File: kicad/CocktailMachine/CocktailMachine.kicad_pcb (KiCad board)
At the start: 2 copper layers, 104.1 x 84.4 mm, 70 parts, among them J1 Conn_01x08_Male, J2 0022232041, J3 3220-10-0100-00, J4 Barrel_Jack_Switch, J5 105-1102-001, J6 105-1103-001, J7 0022232041, U1 ESP32-WROOM-32, U2 TXB0104PWR, U3 MCP6477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

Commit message: Add gerber and drill files
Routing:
- net GND1: track 74.6 -> 74.0 mm
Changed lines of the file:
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@@
       (psa4output false)
       (plotreference true)
-      (plotvalue true)
+      (plotvalue false)
       (plotinvisibletext false)
       (sketchpadsonfab false)
@@
       (outputformat 1)
       (mirror false)
-      (drillshape 1)
+      (drillshape 0)
       (scaleselection 1)
-      (outputdirectory "")
+      (outputdirectory "gerber/")
     )
   )
@@
     (pad "" np_thru_hole circle locked (at 2.046701 4.700001) (size 0.9906 0.9906) (drill 0.9906) (layers *.Cu *.Mask))
     (pad "" np_thru_hole circle locked (at 4.053301 4.700001) (size 0.9906 0.9906) (drill 0.9906) (layers *.Cu *.Mask))
-    (pad "1" thru_hole oval locked (at 6.000001 0 90) (size 4.0132 1.4986) (drill oval 2.7 0.4) (layers *.Cu *.Mask)
+    (pad "1" thru_hole oval locked (at 6.000001 0 90) (size 4.0132 1.4986) (drill oval 2.7 0.4572) (layers *.Cu *.Mask)
       (net 7 "+12V") (pintype "passive"))
-    (pad "2" thru_hole oval locked (at 0 0 90) (size 3.5052 1.4986) (drill oval 2.7 0.4) (layers *.Cu *.Mask)
+    (pad "2" thru_hole oval locked (at 0 0 90) (size 3.5052 1.4986) (drill oval 2.7 0.4572) (layers *.Cu *.Mask)
       (net 6 "GND1") (pintype "passive"))
-    (pad "3" thru_hole oval locked (at 3.050001 4.700001) (size 3.5052 1.4986) (drill oval 2.7 0.4) (layers *.Cu *.Mask)
+    (pad "3" thru_hole oval locked (at 3.050001 4.700001) (size 3.5052 1.4986) (drill oval 2.7 0.4572) (layers *.Cu *.Mask)
       (net 6 "GND1") (pintype "passive"))
   )
@@
   (segment (start 99.5 95.25) (end 99.5 93.275) (width 0.381) (layer "B.Cu") (net 5))
   (segment (start 82.973 67.405) (end 81.703 66.135) (width 0.381) (layer "F.Cu") (net 6))
-  (segment (start 57.660001 75.440001) (end 57.660001 74.550001) (width 0.381) (layer "F.Cu") (net 6))
-  (segment (start 58.42 83.82) (end 59.821591 82.418409) (width 0.381) (layer "F.Cu") (net 6))
+  (segment (start 57.660001 73.889999) (end 57.660001 74.550001) (width 0.381) (layer "F.Cu") (net 6))
   (segment (start 82.338 71.9) (end 82.973 71.265) (width 0.381) (layer "F.Cu") (net 6))
+  (segment (start 57.660001 74.869446) (end 57.660001 74.550001) (width 0.381) (layer "F.Cu") (net 6))
+  (segment (start 59.821591 77.031036) (end 59.821591 82.418409) (width 0.381) (layer "F.Cu") (net 6))
   (segment (start 73.448 72.675) (end 73.943 72.18) (width 0.381) (layer "F.Cu") (net 6))
-  (segment (start 57.660001 74.230556) (end 58.885557 73.005) (width 0.381) (layer "F.Cu") (net 6))
   (segment (start 71.9255 72.675) (end 73.448 72.675) (width 0.381) (layer "F.Cu") (net 6))
   (segment (start 70.7705 73.83) (end 71.9255 72.675) (width 0.381) (layer "F.Cu") (net 6))
-  (segment (start 59.821591 82.418409) (end 59.821591 77.601591) (width 0.381) (layer "F.Cu") (net 6))
   (segment (start 82.973 71.265) (end 82.973 67.405) (width 0.381) (layer "F.Cu") (net 6))
-  (segment (start 54.61 69.85) (end 54.929445 69.85) (width 0.381) (layer "F.Cu") (net 6))
+  (segment (start 55.1053 69.85) (end 57.660001 72.404701) (width 0.381) (layer "F.Cu") (net 6))
   (segment (start 81.068 70.63) (end 82.338 71.9) (width 0.381) (layer "F.Cu") (net 6))
-  (segment (start 57.660001 74.550001) (end 57.660001 74.230556) (width 0.381) (layer "F.Cu") (net 6))
+  (segment (start 59.821591 82.418409) (end 58.42 83.82) (width 0.381) (layer "F.Cu") (net 6))
+  (segment (start 57.95265 72.69735) (end 57.95265 73.59735) (width 0.381) (layer "F.Cu") (net 6))
   (segment (start 58.42 83.82) (end 53.34 83.82) (width 0.381) (layer "F.Cu") (net 6))
+  (segment (start 59.821591 77.031036) (end 57.660001 74.869446) (width 0.381) (layer "F.Cu") (net 6))
+  (segment (start 62.958 73.005) (end 58.2603 73.005) (width 0.381) (layer "F.Cu") (net 6))
   (segment (start 81.068 70.135) (end 81.068 70.63) (width 0.381) (layer "F.Cu") (net 6))
-  (segment (start 58.885557 73.005) (end 62.958 73.005) (width 0.381) (layer "F.Cu") (net 6))
-  (segment (start 59.821591 77.601591) (end 57.660001 75.440001) (width 0.381) (layer "F.Cu") (net 6))
-  (segment (start 54.929445 69.85) (end 57.660001 72.580556) (width 0.381) (layer "F.Cu") (net 6))
+  (segment (start 58.2603 73.005) (end 57.95265 72.69735) (width 0.381) (layer "F.Cu") (net 6))
   (segment (start 73.943 72.04) (end 73.943 70.08415) (width 0.381) (layer "F.Cu") (net 6))
+  (segment (start 57.95265 73.59735) (end 57.660001 73.889999) (width 0.381) (layer "F.Cu") (net 6))
   (segment (start 81.703 66.135) (end 79.25215 66.135) (width 0.381) (layer "F.Cu") (net 6))
-  (segment (start 57.660001 72.580556) (end 57.660001 74.550001) (width 0.381) (layer "F.Cu") (net 6))
+  (segment (start 57.95265 72.69735) (end 57.660001 72.404701) (width 0.381) (layer "F.Cu") (net 6))
   (segment (start 73.943 70.08415) (end 73.79385 69.935) (width 0.381) (layer "F.Cu") (net 6))
+  (segment (start 54.61 69.85) (end 55.1053 69.85) (width 0.381) (layer "F.Cu") (net 6))
   (via (at 73.943 70.08415) (size 0.6604) (drill 0.3302) (layers "F.Cu" "B.Cu") (net 6))
   (via (at 67.158 69.0175) (size 0.8) (drill 0.4) (layers "F.Cu" "B.Cu") (net 6))

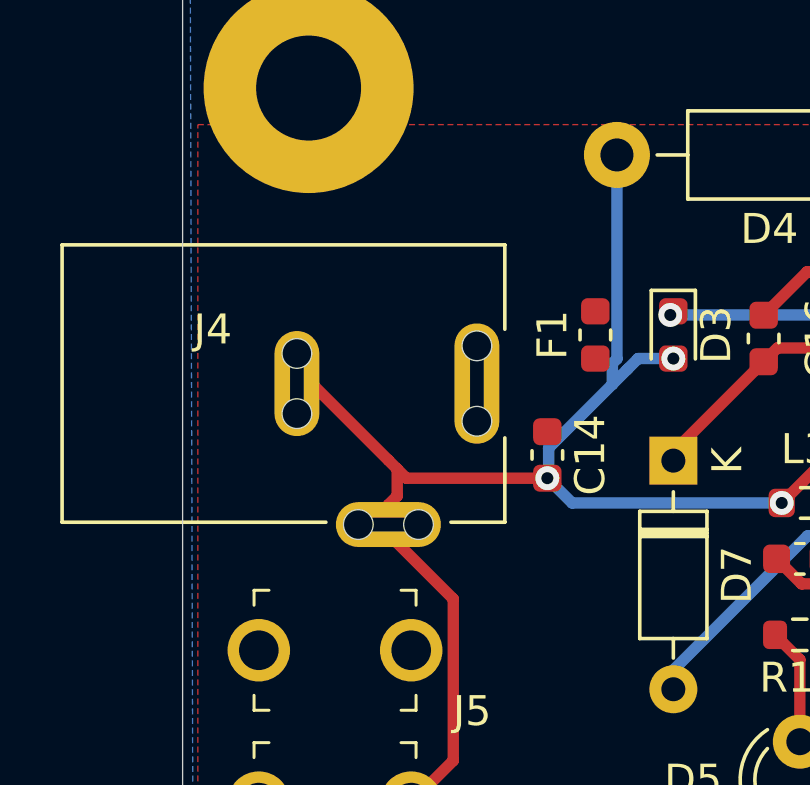
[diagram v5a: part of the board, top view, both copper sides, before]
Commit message: Fix footprint issue
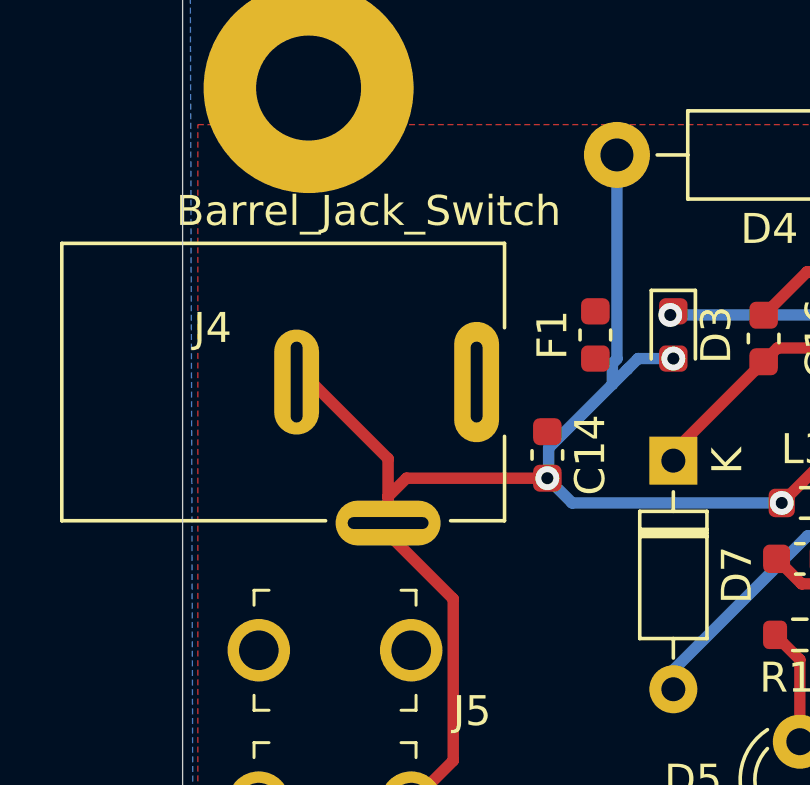
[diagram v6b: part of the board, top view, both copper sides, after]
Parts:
- moved J4 0.05 mm to (54.6, 69.8)
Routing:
- net GND1: track 74.0 -> 74.5 mm
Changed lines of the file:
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@@
       (net 6 "GND1") (pinfunction "SYNC") (pintype "unspecified"))
-  )
-  (footprint "barrel_jack:MJ-180PH" (layer "F.Cu")
-    (at 54.61 69.85)
-    (property "Sheetfile" "power.kicad_sch")
-    (property "Sheetname" "Power")
-    (attr through_hole)
-    (fp_text reference "J4" (at -2.8 -1.8) (layer "F.SilkS")
-      (effects (font (size 1 1) (thickness 0.15)))
-    )
-    (fp_text value "Barrel_Jack_Switch" (at 3.556 -10.414) (layer "F.SilkS") hide
-      (effects (font (size 1 1) (thickness 0.15)))
-    )
-    (fp_text user "*" (at 1.27 -1.27) (layer "F.SilkS") hide
-      (effects (font (size 1 1) (thickness 0.15)))
-    )
-    (fp_text user "Copyright 2021 Accelerated Designs. All rights reserved." (at 0 0) (layer "Cmts.User") hide
-      (effects (font (size 0.127 0.127) (thickness 0.002)))
-    )
-    (fp_text user "*" (at 0 0) (layer "F.Fab")
-      (effects (font (size 1 1) (thickness 0.15)))
-    )
-    (fp_line (start -7.827 4.6228) (end 0.967419 4.6228) (layer "F.SilkS") (width 0.12))
-    (fp_line (start 6.9304 -4.6228) (end -7.827 -4.6228) (layer "F.SilkS") (width 0.12))
-    (fp_line (start 6.9304 -1.80972) (end 6.9304 -4.6228) (layer "F.SilkS") (width 0.12))
-    (fp_line (start 5.132584 4.6228) (end 6.9304 4.6228) (layer "F.SilkS") (width 0.12))
-    (fp_line (start 6.9304 4.6228) (end 6.9304 1.80972) (layer "F.SilkS") (width 0.12))
-    (fp_line (start -7.827 -4.6228) (end -7.827 4.6228) (layer "F.SilkS") (width 0.12))
-    (fp_line (start -7.954 -4.7498) (end 7.0574 -4.7498) (layer "F.CrtYd") (width 0.05))
-    (fp_line (start -7.954 5.703301) (end -7.954 -4.7498) (layer "F.CrtYd") (width 0.05))
-    (fp_line (start 7.0574 5.703301) (end -7.954 5.703301) (layer "F.CrtYd") (width 0.05))
-    (fp_line (start 7.0574 -4.7498) (end 7.0574 5.703301) (layer "F.CrtYd") (width 0.05))
-    (fp_circle (center -8.462 0) (end -8.462 0) (layer "F.CrtYd") (width 0.05) (fill none))
-    (fp_line (start 6.8034 -4.4958) (end -7.7 -4.4958) (layer "F.Fab") (width 0.1))
-    (fp_line (start -7.7 4.4958) (end 6.8034 4.4958) (layer "F.Fab") (width 0.1))
-    (fp_line (start -7.7 -4.4958) (end -7.7 4.4958) (layer "F.Fab") (width 0.1))
-    (fp_line (start 6.8034 4.4958) (end 6.8034 -4.4958) (layer "F.Fab") (width 0.1))
-    (fp_circle (center -6.938 0) (end -6.938 0) (layer "F.Fab") (width 0.1) (fill none))
-    (pad "" np_thru_hole circle locked (at 6.000001 -1.2573) (size 0.9906 0.9906) (drill 0.9906) (layers *.Cu *.Mask))
-    (pad "" np_thru_hole circle locked (at 6.000001 1.2573) (size 0.9906 0.9906) (drill 0.9906) (layers *.Cu *.Mask))
-    (pad "" np_thru_hole circle locked (at 0 -1.0033) (size 0.9906 0.9906) (drill 0.9906) (layers *.Cu *.Mask))
-    (pad "" np_thru_hole circle locked (at 0 1.0033) (size 0.9906 0.9906) (drill 0.9906) (layers *.Cu *.Mask))
-    (pad "" np_thru_hole circle locked (at 2.046701 4.700001) (size 0.9906 0.9906) (drill 0.9906) (layers *.Cu *.Mask))
-    (pad "" np_thru_hole circle locked (at 4.053301 4.700001) (size 0.9906 0.9906) (drill 0.9906) (layers *.Cu *.Mask))
-    (pad "1" thru_hole oval locked (at 6.000001 0 90) (size 4.0132 1.4986) (drill oval 2.7 0.4572) (layers *.Cu *.Mask)
-      (net 7 "+12V") (pintype "passive"))
-    (pad "2" thru_hole oval locked (at 0 0 90) (size 3.5052 1.4986) (drill oval 2.7 0.4572) (layers *.Cu *.Mask)
-      (net 6 "GND1") (pintype "passive"))
-    (pad "3" thru_hole oval locked (at 3.050001 4.700001) (size 3.5052 1.4986) (drill oval 2.7 0.4572) (layers *.Cu *.Mask)
-      (net 6 "GND1") (pintype "passive"))
   )
   (footprint "Resistor_SMD:R_0603_1608Metric" (layer "F.Cu")
@@
       (net 1 "GND") (pinfunction "LED-") (pintype "input"))
   )
+  (footprint "barrel_jack:MJ-180PH" (layer "F.Cu")
+    (at 54.6 69.8)
+    (property "Sheetfile" "power.kicad_sch")
+    (property "Sheetname" "Power")
+    (attr through_hole)
+    (fp_text reference "J4" (at -2.8 -1.8) (layer "F.SilkS")
+      (effects (font (size 1 1) (thickness 0.15)))
+    )
+    (fp_text value "Barrel_Jack_Switch" (at 2.4 -5.7) (layer "F.SilkS")
+      (effects (font (size 1 1) (thickness 0.15)))
+    )
+    (fp_text user "*" (at 0 0) (layer "F.SilkS") hide
+      (effects (font (size 1 1) (thickness 0.15)))
+    )
+    (fp_text user "Copyright 2021 Accelerated Designs. All rights reserved." (at 0 0) (layer "Cmts.User") hide
+      (effects (font (size 0.127 0.127) (thickness 0.002)))
+    )
+    (fp_text user "*" (at 0 0) (layer "F.Fab") hide
+      (effects (font (size 1 1) (thickness 0.15)))
+    )
+    (fp_line (start 6.9304 -1.80972) (end 6.9304 -4.6228) (layer "F.SilkS") (width 0.12))
+    (fp_line (start 6.9304 -4.6228) (end -7.827 -4.6228) (layer "F.SilkS") (width 0.12))
+    (fp_line (start 6.9304 4.6228) (end 6.9304 1.80972) (layer "F.SilkS") (width 0.12))
+    (fp_line (start -7.827 4.6228) (end 0.967419 4.6228) (layer "F.SilkS") (width 0.12))
+    (fp_line (start 5.132584 4.6228) (end 6.9304 4.6228) (layer "F.SilkS") (width 0.12))
+    (fp_line (start -7.827 -4.6228) (end -7.827 4.6228) (layer "F.SilkS") (width 0.12))
+    (fp_line (start -7.954 5.703301) (end -7.954 -4.7498) (layer "F.CrtYd") (width 0.05))
+    (fp_line (start 7.0574 5.703301) (end -7.954 5.703301) (layer "F.CrtYd") (width 0.05))
+    (fp_line (start 7.0574 -4.7498) (end 7.0574 5.703301) (layer "F.CrtYd") (width 0.05))
+    (fp_line (start -7.954 -4.7498) (end 7.0574 -4.7498) (layer "F.CrtYd") (width 0.05))
+    (fp_circle (center -8.462 0) (end -8.462 0) (layer "F.CrtYd") (width 0.05) (fill none))
+    (fp_line (start 6.8034 -4.4958) (end -7.7 -4.4958) (layer "F.Fab") (width 0.1))
+    (fp_line (start 6.8034 4.4958) (end 6.8034 -4.4958) (layer "F.Fab") (width 0.1))
+    (fp_line (start -7.7 4.4958) (end 6.8034 4.4958) (layer "F.Fab") (width 0.1))
+    (fp_line (start -7.7 -4.4958) (end -7.7 4.4958) (layer "F.Fab") (width 0.1))
+    (fp_circle (center -6.938 0) (end -6.938 0) (layer "F.Fab") (width 0.1) (fill none))
+    (pad "1" thru_hole oval (at 6.000001 0 90) (size 4.0132 1.4986) (drill oval 2.7 0.4) (layers *.Cu *.Mask)
+      (net 7 "+12V") (pintype "passive"))
+    (pad "2" thru_hole oval (at 0 0 90) (size 3.5052 1.4986) (drill oval 2.7 0.4) (layers *.Cu *.Mask)
+      (net 6 "GND1") (pintype "passive"))
+    (pad "3" thru_hole oval (at 3.050001 4.700001) (size 3.5052 1.4986) (drill oval 2.7 0.4) (layers *.Cu *.Mask)
+      (net 6 "GND1") (pintype "passive"))
+  )
   (footprint "" (layer "F.Cu")
     (at 55 135)
@@
   (segment (start 99.5 95.25) (end 99.5 93.275) (width 0.381) (layer "B.Cu") (net 5))
   (segment (start 82.973 67.405) (end 81.703 66.135) (width 0.381) (layer "F.Cu") (net 6))
-  (segment (start 57.660001 73.889999) (end 57.660001 74.550001) (width 0.381) (layer "F.Cu") (net 6))
+  (segment (start 54.6 69.8) (end 55.0953 69.8) (width 0.381) (layer "F.Cu") (net 6))
   (segment (start 82.338 71.9) (end 82.973 71.265) (width 0.381) (layer "F.Cu") (net 6))
   (segment (start 57.660001 74.869446) (end 57.660001 74.550001) (width 0.381) (layer "F.Cu") (net 6))
   (segment (start 59.821591 77.031036) (end 59.821591 82.418409) (width 0.381) (layer "F.Cu") (net 6))
   (segment (start 73.448 72.675) (end 73.943 72.18) (width 0.381) (layer "F.Cu") (net 6))
+  (segment (start 58.2603 73.005) (end 57.650001 73.615299) (width 0.381) (layer "F.Cu") (net 6))
   (segment (start 71.9255 72.675) (end 73.448 72.675) (width 0.381) (layer "F.Cu") (net 6))
   (segment (start 70.7705 73.83) (end 71.9255 72.675) (width 0.381) (layer "F.Cu") (net 6))
   (segment (start 82.973 71.265) (end 82.973 67.405) (width 0.381) (layer "F.Cu") (net 6))
-  (segment (start 55.1053 69.85) (end 57.660001 72.404701) (width 0.381) (layer "F.Cu") (net 6))
+  (segment (start 57.650001 73.615299) (end 57.650001 74.500001) (width 0.381) (layer "F.Cu") (net 6))
+  (segment (start 57.650001 74.859446) (end 59.821591 77.031036) (width 0.381) (layer "F.Cu") (net 6))
   (segment (start 81.068 70.63) (end 82.338 71.9) (width 0.381) (layer "F.Cu") (net 6))
   (segment (start 59.821591 82.418409) (end 58.42 83.82) (width 0.381) (layer "F.Cu") (net 6))
-  (segment (start 57.95265 72.69735) (end 57.95265 73.59735) (width 0.381) (layer "F.Cu") (net 6))
+  (segment (start 57.650001 72.354701) (end 57.650001 73.615299) (width 0.381) (layer "F.Cu") (net 6))
   (segment (start 58.42 83.82) (end 53.34 83.82) (width 0.381) (layer "F.Cu") (net 6))
-  (segment (start 59.821591 77.031036) (end 57.660001 74.869446) (width 0.381) (layer "F.Cu") (net 6))
+  (segment (start 81.068 70.135) (end 81.068 70.63) (width 0.381) (layer "F.Cu") (net 6))
+  (segment (start 55.0953 69.8) (end 57.650001 72.354701) (width 0.381) (layer "F.Cu") (net 6))
   (segment (start 62.958 73.005) (end 58.2603 73.005) (width 0.381) (layer "F.Cu") (net 6))
-  (segment (start 81.068 70.135) (end 81.068 70.63) (width 0.381) (layer "F.Cu") (net 6))
-  (segment (start 58.2603 73.005) (end 57.95265 72.69735) (width 0.381) (layer "F.Cu") (net 6))
   (segment (start 73.943 72.04) (end 73.943 70.08415) (width 0.381) (layer "F.Cu") (net 6))
-  (segment (start 57.95265 73.59735) (end 57.660001 73.889999) (width 0.381) (layer "F.Cu") (net 6))
   (segment (start 81.703 66.135) (end 79.25215 66.135) (width 0.381) (layer "F.Cu") (net 6))
-  (segment (start 57.95265 72.69735) (end 57.660001 72.404701) (width 0.381) (layer "F.Cu") (net 6))
   (segment (start 73.943 70.08415) (end 73.79385 69.935) (width 0.381) (layer "F.Cu") (net 6))
-  (segment (start 54.61 69.85) (end 55.1053 69.85) (width 0.381) (layer "F.Cu") (net 6))
+  (segment (start 57.650001 74.500001) (end 57.650001 74.859446) (width 0.381) (layer "F.Cu") (net 6))
   (via (at 73.943 70.08415) (size 0.6604) (drill 0.3302) (layers "F.Cu" "B.Cu") (net 6))
   (via (at 67.158 69.0175) (size 0.8) (drill 0.4) (layers "F.Cu" "B.Cu") (net 6))
